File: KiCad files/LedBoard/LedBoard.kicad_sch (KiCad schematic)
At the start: 20 parts, among them J1 Conn_01x02, J2 Conn_01x02, J3 Conn_01x02, Q1 IRLR120NTRPBF

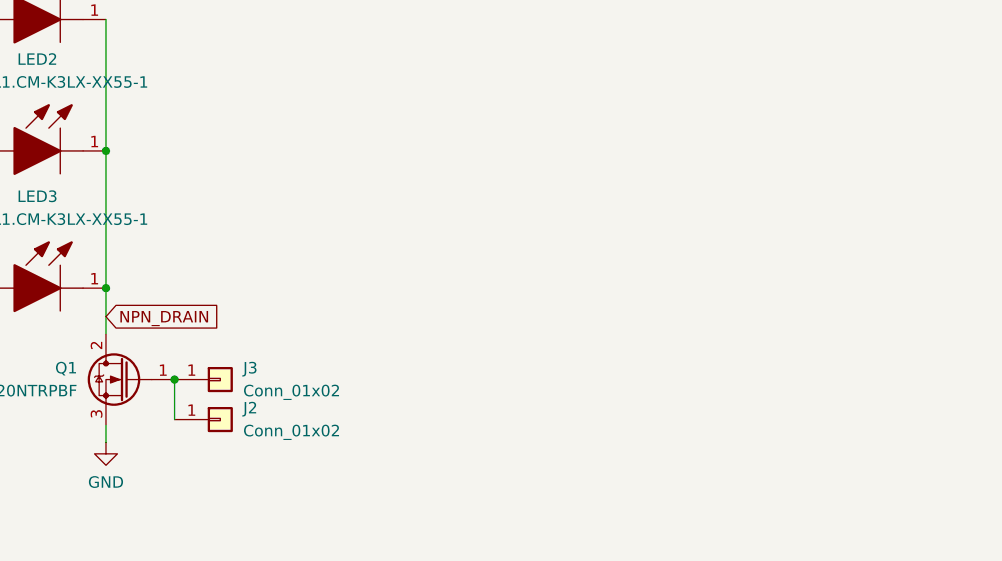
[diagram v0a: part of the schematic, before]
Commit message: changed an XT60 to edge connector because I didnt like the XT60 and pin header setup.
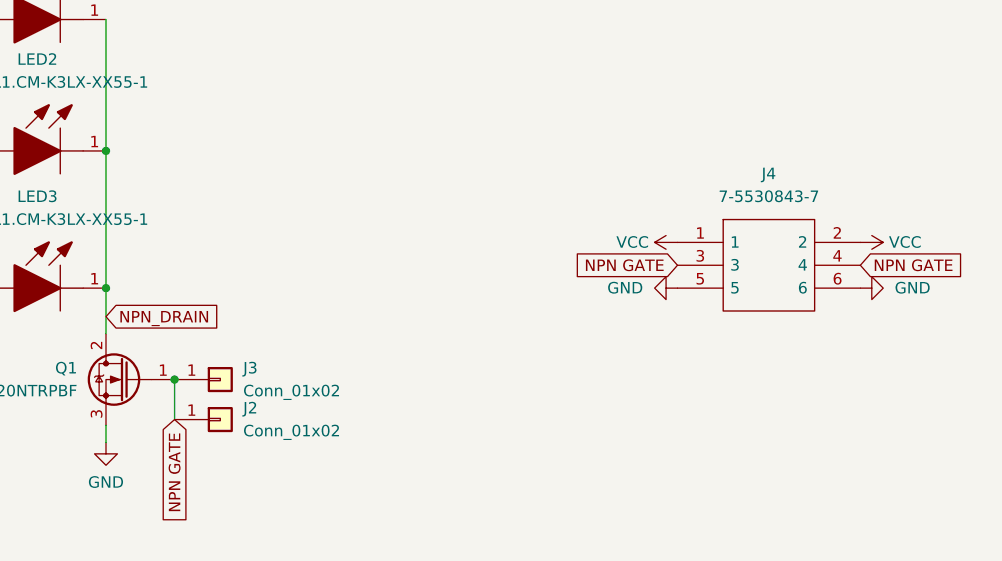
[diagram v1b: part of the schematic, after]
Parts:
- added J4: 7-5530843-7, 7-5530843-7:755308437, symbol 7-5530843-7:7-5530843-7
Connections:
- net GND: now also J4.5, J4.6
- net VCC: now also J4.1, J4.2
- net NPN GATE: now reaches J2.1 (Pin_1), J3.1 (Pin_1), Q1.1 (G)
- net NPN GATE: now also J4.3, J4.4
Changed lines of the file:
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@@
+    )
+  )
+  (global_label "NPN GATE" (shape input) (at 90.17 122.555 270) (fields_autoplaced)
+    (effects (font (size 1.27 1.27)) (justify right))
+    (property "Intersheetrefs" "${INTERSHEET_REFS}" (at 90.17 134.914 90)
+      (effects (font (size 1.27 1.27)) (justify right) hide)
     )
   )
@@
     )
   )
+  (global_label "NPN GATE" (shape input) (at 146.05 105.41 180) (fields_autoplaced)
+    (effects (font (size 1.27 1.27)) (justify right))
+    (property "Intersheetrefs" "${INTERSHEET_REFS}" (at 133.691 105.41 0)
+      (effects (font (size 1.27 1.27)) (justify right) hide)
+    )
+  )
   (global_label "LED_V+" (shape input) (at 67.31 78.105 180) (fields_autoplaced)
     (effects (font (size 1.27 1.27)) (justify right))
@@
     )
   )
+  (global_label "NPN GATE" (shape input) (at 166.37 105.41 0) (fields_autoplaced)
+    (effects (font (size 1.27 1.27)) (justify left))
+    (property "Intersheetrefs" "${INTERSHEET_REFS}" (at 178.729 105.41 0)
+      (effects (font (size 1.27 1.27)) (justify left) hide)
+    )
+  )
+  (symbol (lib_id "power:GND") (at 146.05 107.95 270) (unit 1)
+    (in_bom yes) (on_board yes) (dnp no) (fields_autoplaced)
+    (property "Reference" "#PWR010" (at 139.7 107.95 0)
+      (effects (font (size 1.27 1.27)) hide)
+    )
+    (property "Value" "GND" (at 142.24 107.95 90)
+      (effects (font (size 1.27 1.27)) (justify right))
+    )
+    (property "Footprint" "" (at 146.05 107.95 0)
+      (effects (font (size 1.27 1.27)) hide)
+    )
+    (property "Datasheet" "" (at 146.05 107.95 0)
+      (effects (font (size 1.27 1.27)) hide)
+    )
+    (pin "1")
+    (instances
+      (project "LedBoard"
+        (path "/7007eb9b-f827-4e2f-a1f8-279aa4f63030"
+          (reference "#PWR010") (unit 1)
+        )
+      )
+    )
+  )
   (symbol (lib_id "GW_VJLPL1.CM-K3LX-XX51-1:GW_VJLPL1.CM-K3LX-XX51-1") (at 82.55 92.71 0) (mirror y) (unit 1)
     (in_bom yes) (on_board yes) (dnp no) (fields_autoplaced)
@@
     )
   )
+  (symbol (lib_id "power:VCC") (at 146.05 102.87 90) (unit 1)
+    (in_bom yes) (on_board yes) (dnp no) (fields_autoplaced)
+    (property "Reference" "#PWR05" (at 149.86 102.87 0)
+      (effects (font (size 1.27 1.27)) hide)
+    )
+    (property "Value" "VCC" (at 142.875 102.87 90)
+      (effects (font (size 1.27 1.27)) (justify left))
+    )
+    (property "Footprint" "" (at 146.05 102.87 0)
+      (effects (font (size 1.27 1.27)) hide)
+    )
+    (property "Datasheet" "" (at 146.05 102.87 0)
+      (effects (font (size 1.27 1.27)) hide)
+    )
+    (pin "1")
+    (instances
+      (project "LedBoard"
+        (path "/7007eb9b-f827-4e2f-a1f8-279aa4f63030"
+          (reference "#PWR05") (unit 1)
+        )
+      )
+    )
+  )
   (symbol (lib_id "power:GND") (at 49.53 51.435 0) (unit 1)
     (in_bom yes) (on_board yes) (dnp no) (fields_autoplaced)
@@
         (path "/d80cef19-75ee-4cfe-8d31-e56b6cad8d97"
           (reference "#PWR0102") (unit 1)
+        )
+      )
+    )
+  )
+  (symbol (lib_id "power:VCC") (at 166.37 102.87 270) (mirror x) (unit 1)
+    (in_bom yes) (on_board yes) (dnp no) (fields_autoplaced)
+    (property "Reference" "#PWR011" (at 162.56 102.87 0)
+      (effects (font (size 1.27 1.27)) hide)
+    )
+    (property "Value" "VCC" (at 169.545 102.87 90)
+      (effects (font (size 1.27 1.27)) (justify left))
+    )
+    (property "Footprint" "" (at 166.37 102.87 0)
+      (effects (font (size 1.27 1.27)) hide)
+    )
+    (property "Datasheet" "" (at 166.37 102.87 0)
+      (effects (font (size 1.27 1.27)) hide)
+    )
+    (pin "1")
+    (instances
+      (project "LedBoard"
+        (path "/7007eb9b-f827-4e2f-a1f8-279aa4f63030"
+          (reference "#PWR011") (unit 1)
         )
       )
@@
     )
   )
+  (symbol (lib_id "power:GND") (at 166.37 107.95 90) (mirror x) (unit 1)
+    (in_bom yes) (on_board yes) (dnp no) (fields_autoplaced)
+    (property "Reference" "#PWR012" (at 172.72 107.95 0)
+      (effects (font (size 1.27 1.27)) hide)
+    )
+    (property "Value" "GND" (at 170.18 107.95 90)
+      (effects (font (size 1.27 1.27)) (justify right))
+    )
+    (property "Footprint" "" (at 166.37 107.95 0)
+      (effects (font (size 1.27 1.27)) hide)
+    )
+    (property "Datasheet" "" (at 166.37 107.95 0)
+      (effects (font (size 1.27 1.27)) hide)
+    )
+    (pin "1")
+    (instances
+      (project "LedBoard"
+        (path "/7007eb9b-f827-4e2f-a1f8-279aa4f63030"
+          (reference "#PWR012") (unit 1)
+        )
+      )
+    )
+  )
   (symbol (lib_id "Mechanical:MountingHole_Pad") (at 30.48 86.36 0) (unit 1)
     (in_bom yes) (on_board yes) (dnp no) (fields_autoplaced)
@@
         )
       )
+    )
+  )
+  (symbol (lib_id "7-5530843-7:7-5530843-7") (at 146.05 102.87 0) (unit 1)
+    (in_bom yes) (on_board yes) (dnp no) (fields_autoplaced)
+    (property "Reference" "J4" (at 156.21 95.25 0)
+      (effects (font (size 1.27 1.27)))
+    )
+    (property "Value" "7-5530843-7" (at 156.21 97.79 0)
+      (effects (font (size 1.27 1.27)))
+    )
+    (property "Footprint" "7-5530843-7:755308437" (at 162.56 100.33 0)
+      (effects (font (size 1.27 1.27)) (justify left) hide)
+    )
+    (property "Datasheet" "https://www.te.com/commerce/DocumentDelivery/DDEController?Action=srchrtrv&DocNm=1773096_SEC03_CARD_EDGE&DocType=CS&DocLang=English" (at 162.56 102.87 0)
+      (effects (font (size 1.27 1.27)) (justify left) hide)
+    )
+    (property "Description" "Standard Card Edge Connectors CONN SEC II 3 POS 100C/L" (at 162.56 105.41 0)
+      (effects (font (size 1.27 1.27)) (justify left) hide)
+    )
+    (property "Height" "15.494" (at 162.56 107.95 0)
+      (effects (font (size 1.27 1.27)) (justify left) hide)
+    )
+    (property "Mouser Part Number" "571-7-5530843-7" (at 162.56 110.49 0)
+      (effects (font (size 1.27 1.27)) (justify left) hide)
+    )
+    (property "Mouser Price/Stock" "https://www.mouser.co.uk/ProductDetail/TE-Connectivity/7-5530843-7?qs=D%2FjeFm%2FW2iQ1%2F6zLIVw4Pg%3D%3D" (at 162.56 113.03 0)
+      (effects (font (size 1.27 1.27)) (justify left) hide)
+    )
+    (property "Manufacturer_Name" "TE Connectivity" (at 162.56 115.57 0)
+      (effects (font (size 1.27 1.27)) (justify left) hide)
+    )
+    (property "Manufacturer_Part_Number" "7-5530843-7" (at 162.56 118.11 0)
+      (effects (font (size 1.27 1.27)) (justify left) hide)
+    )
+    (pin "1")
+    (pin "5")
+    (pin "3")
+    (pin "2")
+    (pin "4")
+    (pin "6")
+    (instances
+      (project "LedBoard"
+        (path "/7007eb9b-f827-4e2f-a1f8-279aa4f63030"
+          (reference "J4") (unit 1)
+        )
+      )

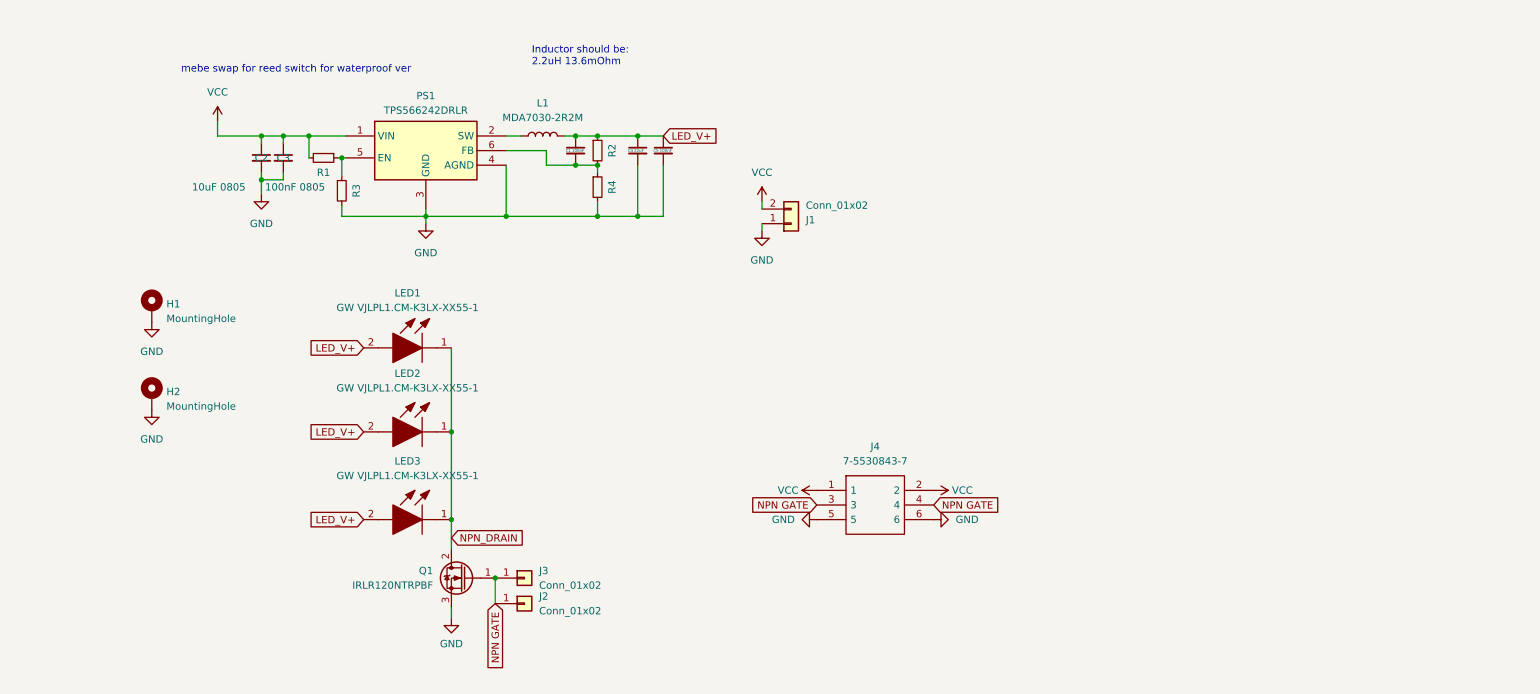
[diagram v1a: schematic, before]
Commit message: added footprints for some discontinued LEDs i have spare of, added level shifter to ensure gate voltage is above threshold
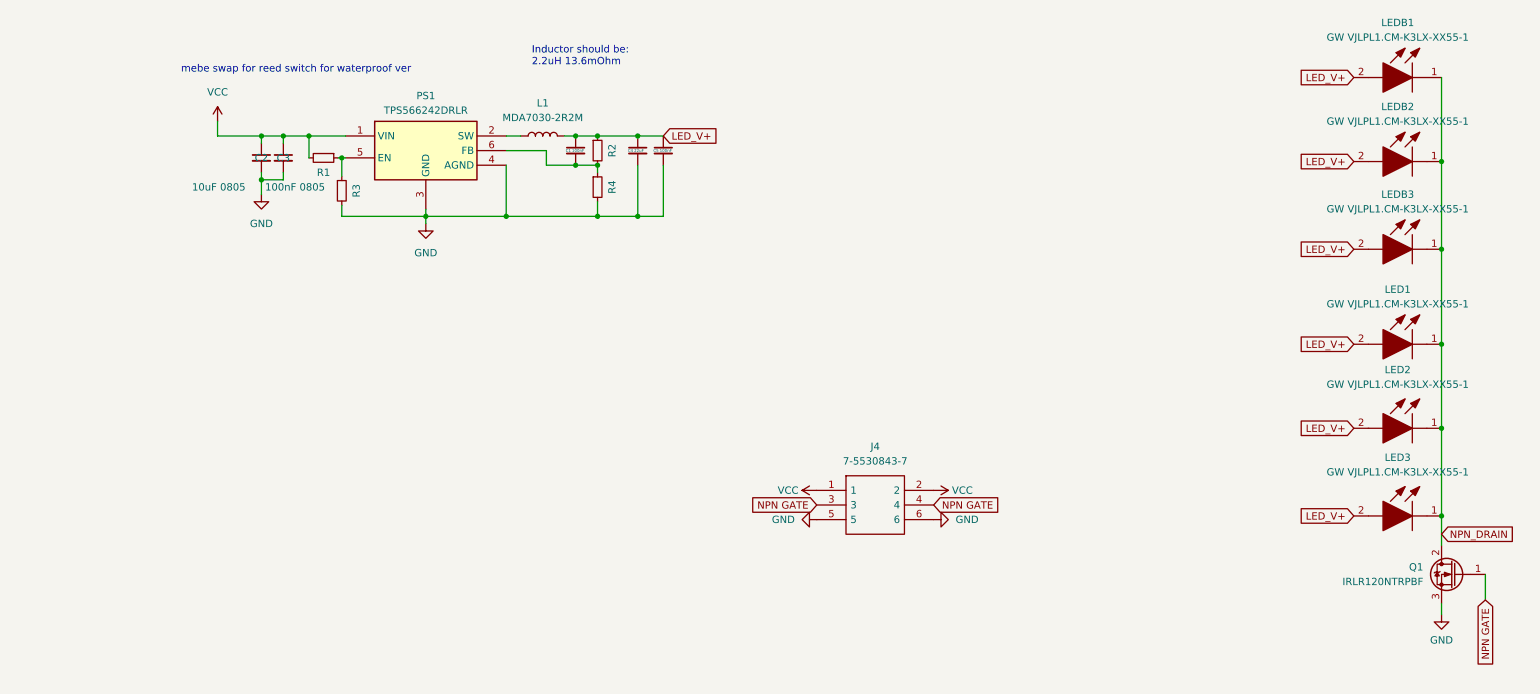
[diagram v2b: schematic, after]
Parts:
- removed H1, H2: MountingHole, MountingHole:MountingHole_2.2mm_M2_DIN965_Pad, symbol Mechanical:MountingHole_Pad
- removed J1: Conn_01x02, Connector_AMASS:AMASS_XT60-F_1x02_P7.20mm_Vertical, symbol Connector_Generic:Conn_01x02
- removed J2, J3: Conn_01x02, Connector_PinSocket_2.54mm:PinSocket_1x01_P2.54mm_Vertical, symbol Connector_Generic:Conn_01x01
- added LEDB1, LEDB2, LEDB3: GW VJLPL1.CM-K3LX-XX55-1, GWVJLPL1CMK3LXXX511:GWVJLPL1CMK3LXXX511, symbol GW_VJLPL1.CM-K3LX-XX51-1:GW_VJLPL1.CM-K3LX-XX51-1
- LED1, LED2, LED3: footprint GWVJLPL1CMK3LXXX511:GWVJLPL1CMK3LXXX511 -> GW_VJLPE1:GW_VJLPE1.CM_0.91x0.91mm
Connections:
- net LED_V+: now also LEDB1.2, LEDB2.2, LEDB3.2
- net NPN_DRAIN: now also LEDB1.1, LEDB2.1, LEDB3.1
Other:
- moved on the sheet: LED1, LED2, LED3, Q1

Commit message: some partial work towards modifying the design yet again
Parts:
- removed C1, C5: 100nF, Capacitor_SMD:C_0805_2012Metric, symbol Device:C_Small
- removed C2: 10uF 0805, Capacitor_SMD:C_0805_2012Metric, symbol Device:C_Small
- removed C3: 100nF 0805, Capacitor_SMD:C_0805_2012Metric, symbol Device:C_Small
- removed C4: 22uF, Capacitor_SMD:C_0805_2012Metric, symbol Device:C_Small
- removed L1: MDA7030-2R2M, Inductor_SMD:L_Coilcraft_XAL7030-222, symbol Device:L
- removed PS1: TPS566242DRLR, Package_TO_SOT_SMD:SOT-563, symbol TPS566242DRLR:TPS566242DRLR
- removed R1: 100K 0805, Resistor_SMD:R_0805_2012Metric, symbol Device:R_Small
- removed R2: 120K 0805, Resistor_SMD:R_0805_2012Metric, symbol Device:R_Small
- removed R3: 23.2K 0805, Resistor_SMD:R_0805_2012Metric, symbol Device:R_Small
- removed R4: 30K 0805, Resistor_SMD:R_0805_2012Metric, symbol Device:R_Small
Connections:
- net LED_V+ is gone; now on net VCC: LED1.2, LED2.2, LED3.2, LEDB1.2, LEDB2.2, LEDB3.2
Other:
- note removed: "Inductor should be: 2.2uH 13.6mOhm"
- note removed: "mebe swap for reed switch for waterproof ver"

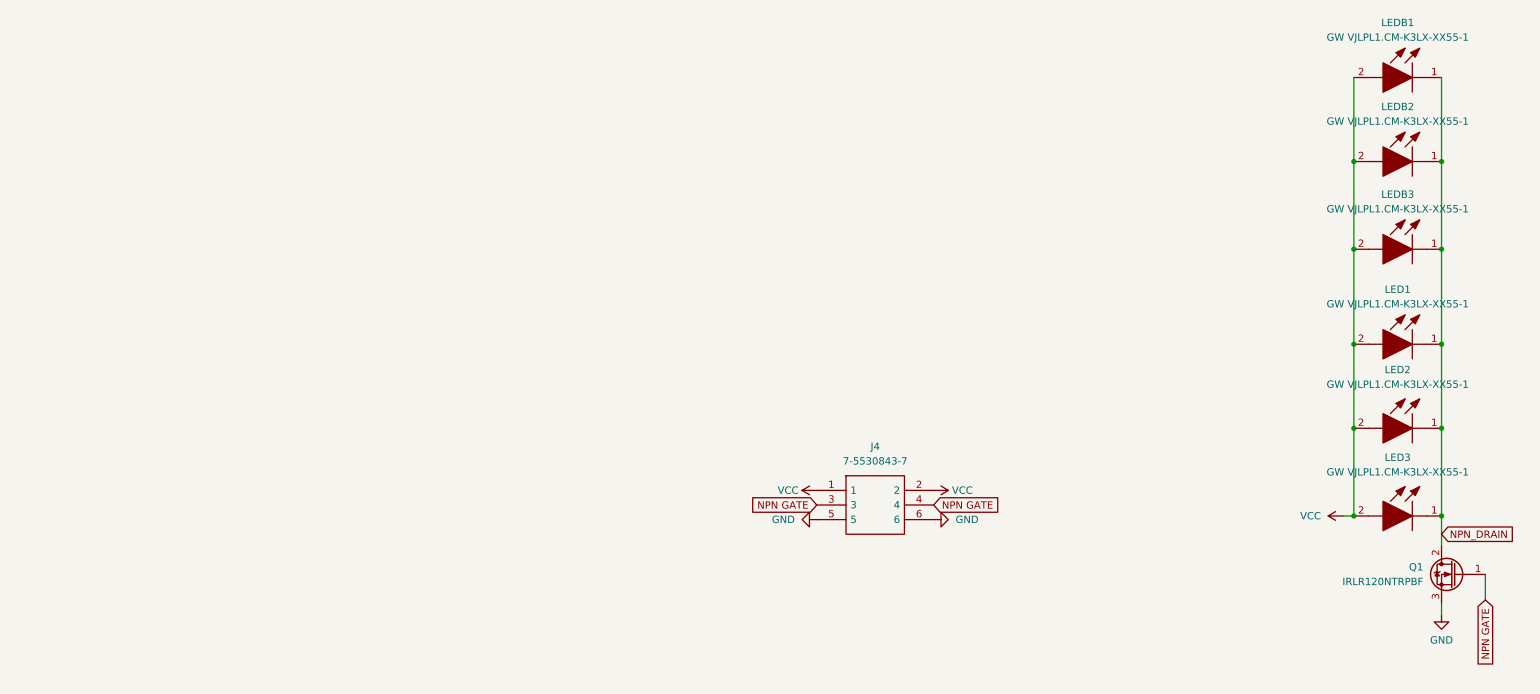
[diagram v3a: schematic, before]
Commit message: updated LED board to use new LEDs
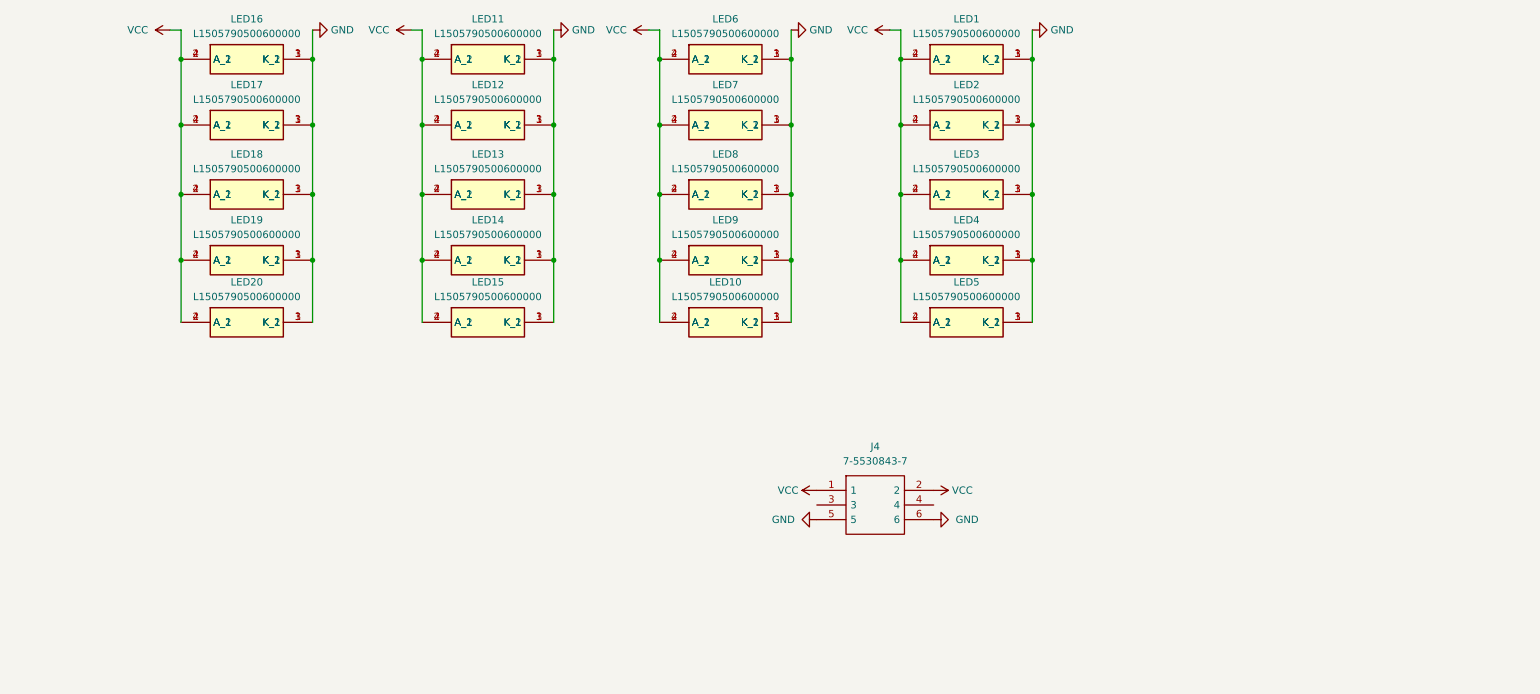
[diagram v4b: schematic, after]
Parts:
- removed LED1, LED2, LED3: GW VJLPL1.CM-K3LX-XX55-1, GW_VJLPE1:GW_VJLPE1.CM_0.91x0.91mm, symbol GW_VJLPL1.CM-K3LX-XX51-1:GW_VJLPL1.CM-K3LX-XX51-1
- removed LEDB2, LEDB3: GW VJLPL1.CM-K3LX-XX55-1, GWVJLPL1CMK3LXXX511:GWVJLPL1CMK3LXXX511, symbol GW_VJLPL1.CM-K3LX-XX51-1:GW_VJLPL1.CM-K3LX-XX51-1
- removed Q1: IRLR120NTRPBF, Package_TO_SOT_SMD:TO-252-2, symbol Device:Q_NMOS_Depletion_GDS
- added LED10, LED11, LED12, LED13, LED14, LED15, LED16, LED17, LED18, LED19, LED2, LED20, LED3, LED4, LED5, LED6, LED7, LED8, LED9: L1505790500600000, L150-5790500600000:L1505790500600000, symbol L150-5790500600000:L150-5790500600000
- LED1: renamed from LEDB1; value GW VJLPL1.CM-K3LX-XX55-1 -> L1505790500600000; footprint GWVJLPL1CMK3LXXX511:GWVJLPL1CMK3LXXX511 -> L150-5790500600000:L1505790500600000; symbol GW_VJLPL1.CM-K3LX-XX51-1:GW_VJLPL1.CM-K3LX-XX51-1 -> L150-5790500600000:L150-5790500600000; Height 0.85 -> (none); Manufacturer_Name ams OSRAM -> (none); Manufacturer_Part_Number GW VJLPL1.CM-K3LX-XX51-1 -> (none)
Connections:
- net NPN_DRAIN is gone; now on net GND: LED1.1 (K_1)
- net GND: now also LED1.3 (K_2), LED10.1 (K_1), LED10.3 (K_2), LED11.1 (K_1), LED11.3 (K_2), LED12.1 (K_1), LED12.3 (K_2), LED13.1 (K_1), LED13.3 (K_2), LED14.1 (K_1), LED14.3 (K_2), LED15.1 (K_1), LED15.3 (K_2), LED16.1 (K_1), LED16.3 (K_2), LED17.1 (K_1), LED17.3 (K_2), LED18.1 (K_1), LED18.3 (K_2), LED19.1 (K_1), LED19.3 (K_2), LED2.1 (K_1), LED2.3 (K_2), LED20.1 (K_1), LED20.3 (K_2), LED3.1 (K_1), LED3.3 (K_2), LED4.1 (K_1), LED4.3 (K_2), LED5.1 (K_1), LED5.3 (K_2), LED6.1 (K_1), LED6.3 (K_2), LED7.1 (K_1), LED7.3 (K_2), LED8.1 (K_1), LED8.3 (K_2), LED9.1 (K_1), LED9.3 (K_2)
- net VCC: now also LED1.4 (A_2), LED10.2 (A_1), LED10.4 (A_2), LED11.2 (A_1), LED11.4 (A_2), LED12.2 (A_1), LED12.4 (A_2), LED13.2 (A_1), LED13.4 (A_2), LED14.2 (A_1), LED14.4 (A_2), LED15.2 (A_1), LED15.4 (A_2), LED16.2 (A_1), LED16.4 (A_2), LED17.2 (A_1), LED17.4 (A_2), LED18.2 (A_1), LED18.4 (A_2), LED19.2 (A_1), LED19.4 (A_2), LED2.2 (A_1), LED2.4 (A_2), LED20.2 (A_1), LED20.4 (A_2), LED3.2 (A_1), LED3.4 (A_2), LED4.2 (A_1), LED4.4 (A_2), LED5.2 (A_1), LED5.4 (A_2), LED6.2 (A_1), LED6.4 (A_2), LED7.2 (A_1), LED7.4 (A_2), LED8.2 (A_1), LED8.4 (A_2), LED9.2 (A_1), LED9.4 (A_2)
- net NPN GATE: no longer names the net of J4.3
- net NPN GATE: no longer J4.4

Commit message: re-organised some files, started work on implementing 100W and 240W EPR versions of the charge board
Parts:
- LED1, LED10, LED11, LED12, LED13, LED14, LED15, LED16, LED17, LED18, LED19, LED2, LED20, LED3, LED4, LED5, LED6, LED7, LED8, LED9: footprint L150-5790500600000:L1505790500600000 -> L150-57705024000H0
